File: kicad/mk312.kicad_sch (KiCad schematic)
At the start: 0 parts

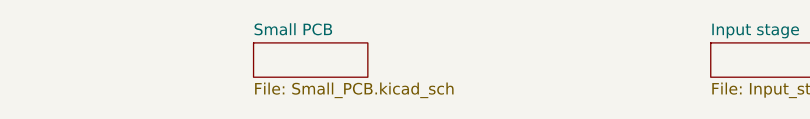
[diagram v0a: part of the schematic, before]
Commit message: Conversion of display print to KiCad components; still attached to main board
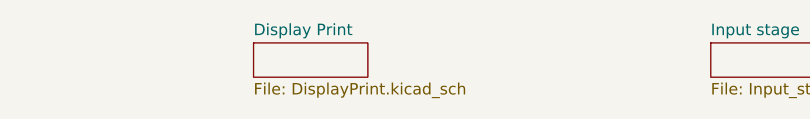
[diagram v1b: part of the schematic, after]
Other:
- sheet Small PCB renamed Display Print
- sheet Display Print: file Small_PCB.kicad_sch -> DisplayPrint.kicad_sch
